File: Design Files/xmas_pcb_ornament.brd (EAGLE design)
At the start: 58.4 x 68 mm, 23 parts, among them Q1 220mA/50V/3.5Ω, U1 ATTINY85

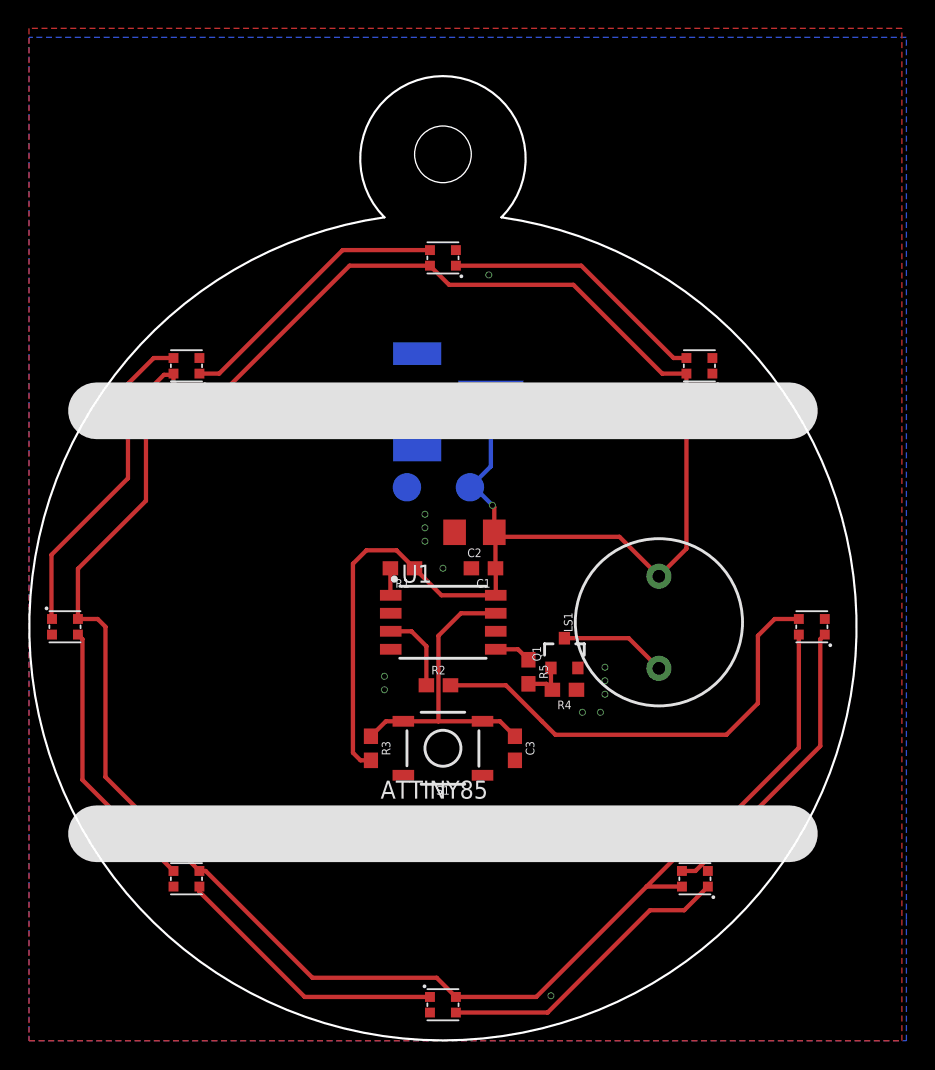
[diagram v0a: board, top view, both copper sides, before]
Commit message: Changed placement of the stripes and JST connector.
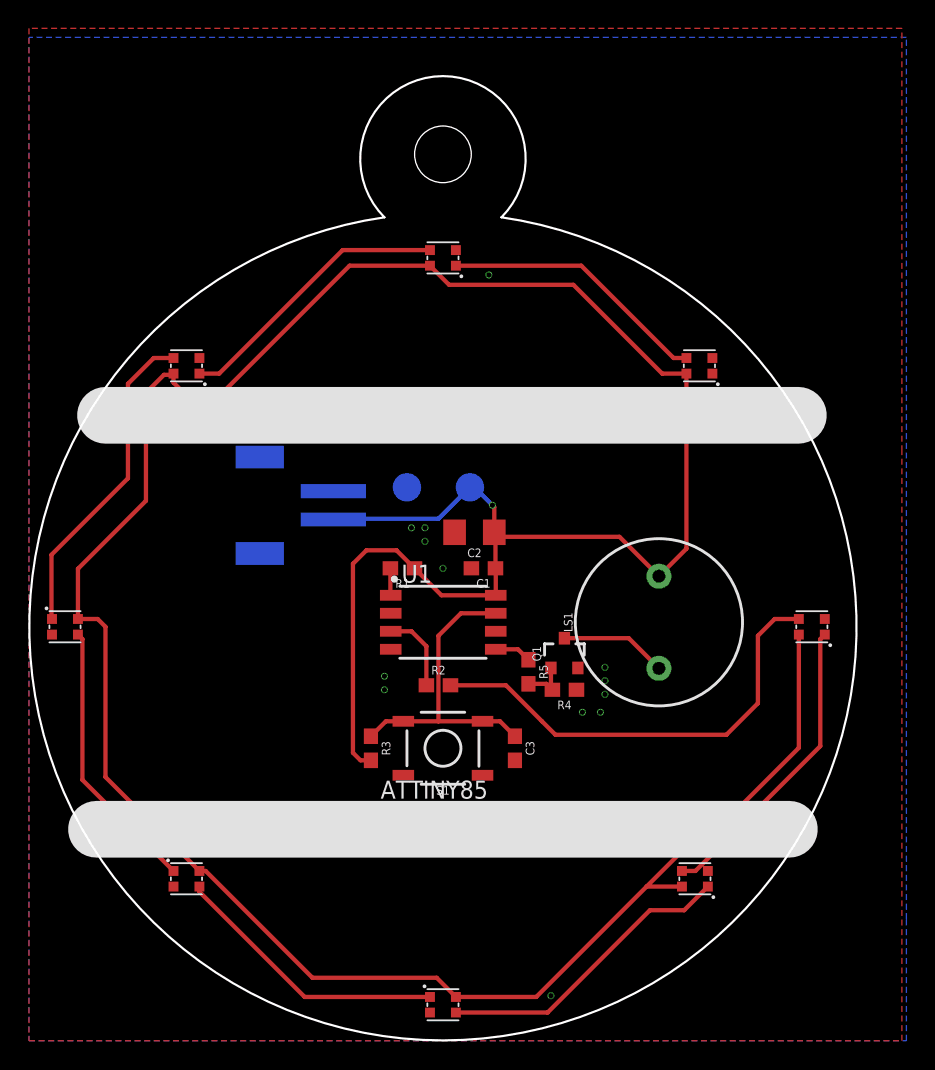
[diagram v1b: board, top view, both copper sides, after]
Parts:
- moved J1 13.3 mm to (17.8, 37.8)
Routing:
- net VCC: track 218.9 -> 223.9 mm
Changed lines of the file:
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@@
 <layer number="156" name="BoardOutline" color="60" fill="1" visible="yes" active="yes"/>
 <layer number="157" name="Helpers" color="7" fill="1" visible="yes" active="yes"/>
-<layer number="158" name="topSilk" color="7" fill="1" visible="no" active="yes"/>
+<layer number="158" name="topSilk" color="7" fill="1" visible="yes" active="yes"/>
 <layer number="159" name="bottomSilk" color="7" fill="1" visible="yes" active="yes"/>
 <layer number="166" name="AntennaArea" color="7" fill="1" visible="no" active="no"/>
@@
 <wire x1="29.21" y1="29.5275" x2="-1.27" y2="-0.9525" width="0.3048" layer="157"/>
 <wire x1="-1.27" y1="-0.9525" x2="-1.27" y2="-1.905" width="0.3048" layer="157"/>
-<wire x1="4.7625" y1="44.45" x2="53.6575" y2="44.45" width="4" layer="158"/>
-<wire x1="4.7625" y1="14.605" x2="53.6575" y2="14.605" width="4" layer="158"/>
-<wire x1="4.7625" y1="44.45" x2="53.6575" y2="44.45" width="4" layer="159"/>
-<wire x1="4.445" y1="14.605" x2="53.6575" y2="14.605" width="4" layer="159"/>
+<wire x1="5.3975" y1="44.1325" x2="54.2925" y2="44.1325" width="4" layer="158"/>
+<wire x1="4.7625" y1="14.9225" x2="53.6575" y2="14.9225" width="4" layer="158"/>
+<wire x1="5.3975" y1="44.1325" x2="54.2925" y2="44.1325" width="4" layer="159"/>
+<wire x1="4.445" y1="14.9225" x2="53.6575" y2="14.9225" width="4" layer="159"/>
 <text x="29.21" y="1.905" size="0.8128" layer="159" font="vector" rot="MR0" align="center">Borna Biro
 5.12.2022.</text>
@@
 <attribute name="VALUE" x="34.4805" y="26.035" size="0.6096" layer="27" font="vector" ratio="20" rot="R270" align="top-center"/>
 </element>
-<element name="J1" library="SparkFun-Connectors" package="JST-2-SMD" value="" x="28.8925" y="45.085" smashed="yes" rot="MR270">
-<attribute name="NAME" x="27.1145" y="46.482" size="0.6096" layer="26" font="vector" ratio="20" rot="MR270"/>
-<attribute name="PROD_ID" value="CONN-11443" x="28.8925" y="45.085" size="5.08" layer="28" font="vector" rot="MR270" display="off"/>
-<attribute name="SF_ID" value="PRT-08612" x="28.8925" y="45.085" size="5.08" layer="28" font="vector" rot="MR270" display="off"/>
-<attribute name="VALUE" x="28.2575" y="46.736" size="0.6096" layer="28" font="vector" ratio="20" rot="MR270"/>
+<element name="J1" library="SparkFun-Connectors" package="JST-2-SMD" value="" x="17.78" y="37.7825" smashed="yes" rot="MR270">
+<attribute name="NAME" x="16.002" y="39.1795" size="0.6096" layer="26" font="vector" ratio="20" rot="MR270"/>
+<attribute name="PROD_ID" value="CONN-11443" x="17.78" y="37.7825" size="5.08" layer="28" font="vector" rot="MR270" display="off"/>
+<attribute name="SF_ID" value="PRT-08612" x="17.78" y="37.7825" size="5.08" layer="28" font="vector" rot="MR270" display="off"/>
+<attribute name="VALUE" x="17.145" y="39.4335" size="0.6096" layer="28" font="vector" ratio="20" rot="MR270"/>
 </element>
 </elements>
@@
 <wire x1="32.8325" y1="37.6525" x2="32.8325" y2="35.8775" width="0.3048" layer="1"/>
 <contactref element="J1" pad="2"/>
-<wire x1="32.5925" y1="44.085" x2="32.5925" y2="40.53" width="0.3048" layer="16"/>
-<wire x1="32.5925" y1="40.53" x2="31.115" y2="39.0525" width="0.3048" layer="16"/>
+<wire x1="31.115" y1="39.0525" x2="28.8925" y2="36.83" width="0.3048" layer="16"/>
+<wire x1="28.8925" y1="36.83" x2="21.5275" y2="36.83" width="0.3048" layer="16"/>
+<wire x1="21.5275" y1="36.83" x2="21.48" y2="36.7825" width="0.3048" layer="16"/>
 </signal>
 <signal name="GND">
@@
 <via x="27.94" y="36.195" extent="1-16" drill="0.35"/>
 <via x="27.94" y="35.2425" extent="1-16" drill="0.35"/>
-<via x="27.94" y="37.1475" extent="1-16" drill="0.35"/>
+<via x="26.9875" y="36.195" extent="1-16" drill="0.35"/>
 <via x="29.21" y="33.3375" extent="1-16" drill="0.35"/>
 <via x="25.0825" y="25.7175" extent="1-16" drill="0.35"/>
